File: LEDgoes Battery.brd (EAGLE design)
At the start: 36.8 x 54 mm, 29 parts, among them U1 TPS61032

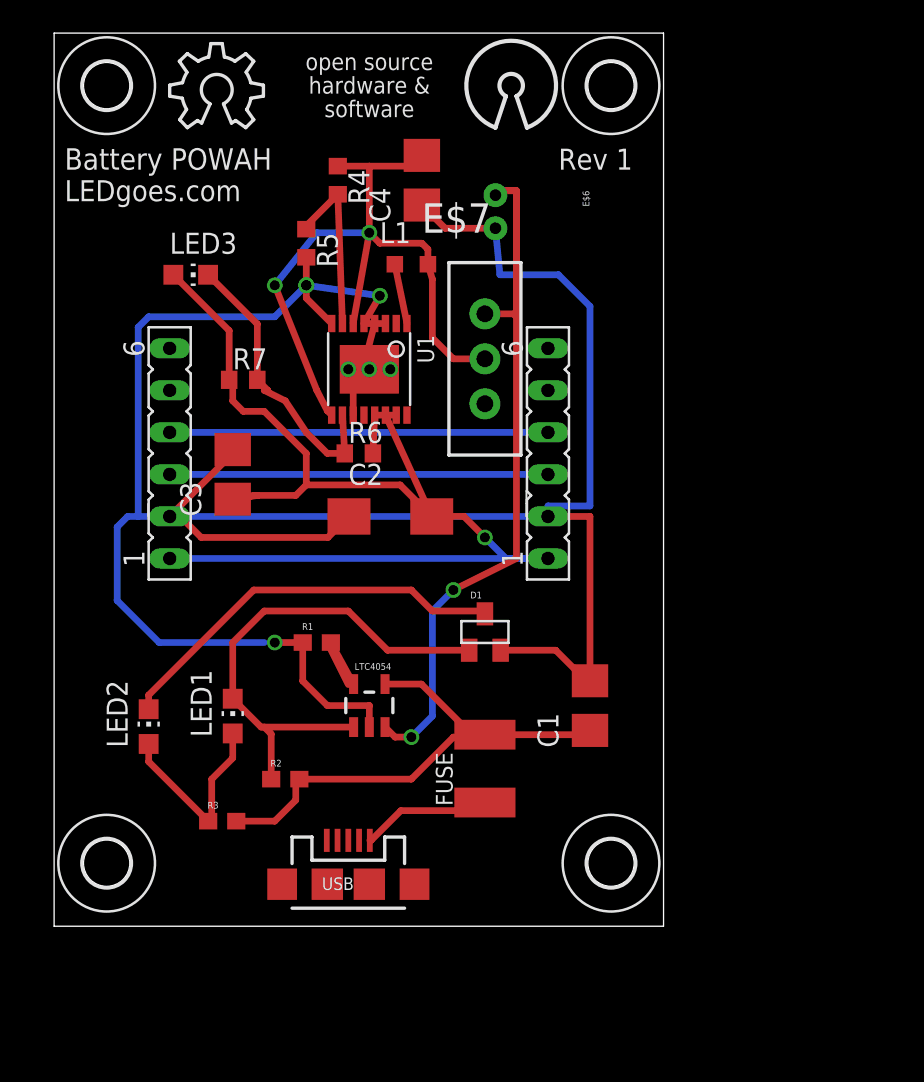
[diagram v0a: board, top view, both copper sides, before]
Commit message: Revision 1 - First Production Revision
Passed design review check 3/2/14
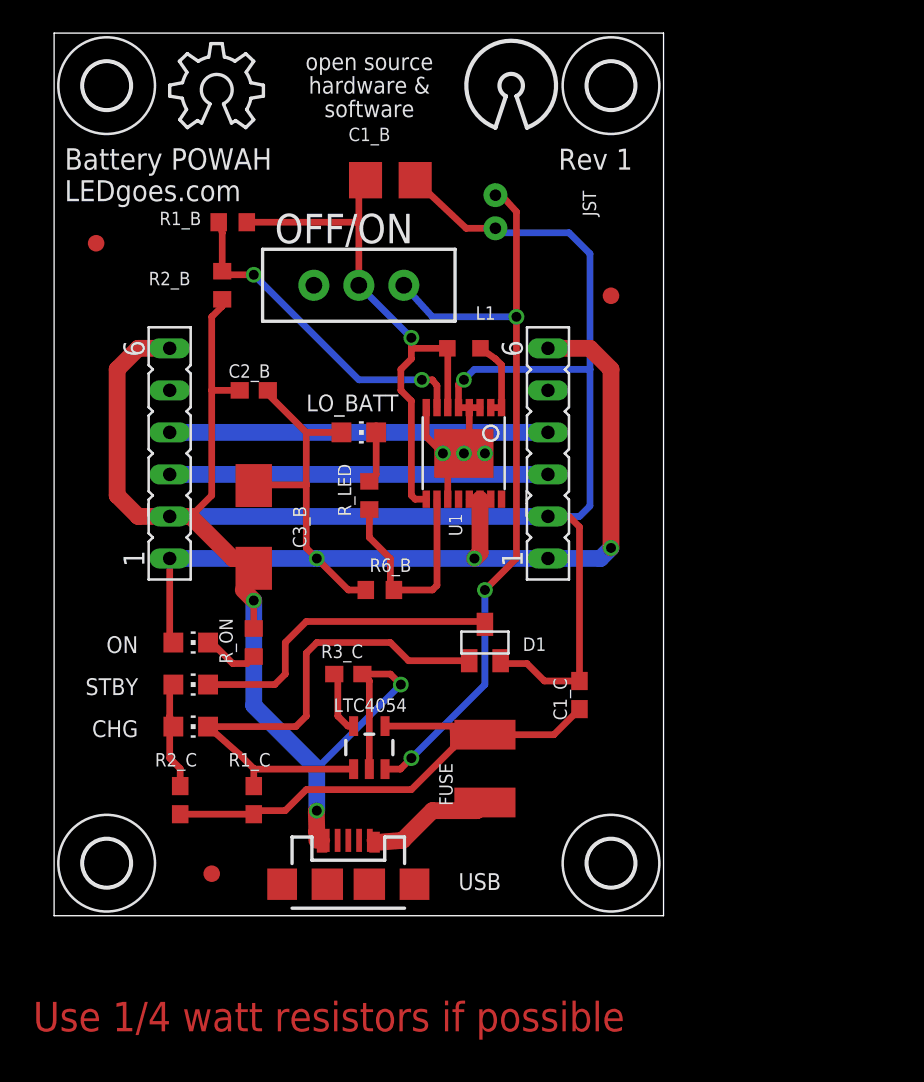
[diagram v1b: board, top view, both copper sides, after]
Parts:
- removed C1: 1uf, rcl:CT3528
- removed C2: 220uF, ref-packages:CT6032
- removed C3: 2.2uf, ref-packages:CT3528
- removed C4: 10uf, ref-packages:CT3528
- removed E$7: (no value), SparkFun-Electromechanical:SWITCH-SPDT_KIT
- removed LED1: Charge, led:CHIP-LED0805
- removed LED2: Standby, led:CHIP-LED0805
- removed LED3: Output, led:CHIP-LED0805
- removed R1: 2k, SparkFun-Resistors:0603
- removed R2: 10k, SparkFun-Resistors:0603
- removed R3: 1k, SparkFun-Resistors:0603
- removed R4, R5, R6, R7: (no value), eagle-ltspice:R0603
- added C1_B: 10uf, ref-packages:CT3528
- added C1_C: 1uf, adafruit:C0603
- added C2_B: 2.2uf, adafruit:C0603
- added C3_B: 220uF, ref-packages:CT6032
- added CHG, LO_BATT, ON, STBY: (no value), led:CHIP-LED0805
- added E$10, E$8, E$9: (no value), adafruit:FIDUCIAL_1MM
- added OFF/ON: (no value), SparkFun-Electromechanical:SWITCH-SPDT_KIT
- added R1_B, R2_B, R6_B, R_LED, R_ON: (no value), eagle-ltspice:R0603
- added R1_C: 10k, SparkFun-Resistors:0603
- added R2_C: 1k, SparkFun-Resistors:0603
- added R3_C: 2k, SparkFun-Resistors:0603
- moved U1 7.65 mm to (25.4, 29.2)
- moved L1 5.99 mm to (25.4, 35.6), turned to 180 degrees
- moved LTC4054 2.54 mm to (19.7, 11.4)
- moved D1 0.63 mm to (26.7, 17.8)
- renumbered E$6 to JST
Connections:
- net S$6 renamed S$20
- removed net S$12: LTC4054.3
- removed net S$13: D1.1, LED1.C, LTC4054.1, R2.1
- removed net S$18: R4.2, R5.1, U1.7
- removed net S$19: C4.-, E$7.2, L1.2, R4.1, U1.6, U1.9
- removed net S$21: L1.1, U1.1
- removed net S$22: C1.-, C2.+, C3.-, C4.+, D1.2, JST.2, LTC4054.2, R1.1, R5.2, U1.11, U1.3, U1.4, U1.5, U1.8, U1.EXP, _.2, __.2
- removed net S$27: C2.-, C3.+, LED3.A, R6.2, R7.1, U1.13, U1.14, U1.15, _.1, __.1
- removed net S$28: LED3.C, R6.1, R7.2, U1.10
- new net /CHRG: CHG.C, D1.1, LTC4054.1, R1_C.1
- new net EN: C1_B.-, L1.2, OFF/ON.2, R1_B.1, U1.6, U1.9
- new net GND: C1_B.+, C1_C.2, C2_B.1, C3_B.+, D1.2, JST.2, LTC4054.2, R2_B.2, R3_C.1, R_ON.2, U1.3, U1.4, U1.5, U1.EXP, USB.VBUS, _.2, _.6, __.2
- new net LBI: R1_B.2, R2_B.1, U1.7
- new net LBO: R6_B.1, R_LED.2, U1.10
- new net S$1: ON.C, R_ON.1
- new net SW: L1.1, U1.1, U1.2
- new net VCC: FUSE.1, USB.GND
- new net VCC_FUSED: C1_C.1, FUSE.2, LTC4054.4, R1_C.2, R2_C.2
- new net VOUT: C2_B.2, C3_B.-, LO_BATT.A, ON.A, R6_B.2, U1.13, U1.14, U1.15, _.1, __.1, __.6
- net S$10: now also LO_BATT.C, R_LED.1; no longer C1.+, FUSE.2, LTC4054.4, R2.2, R3.2
- net S$11: now also R3_C.2; no longer R1.2
- net S$15: now also CHG.A, R2_C.1, STBY.A; no longer LED1.A, LED2.A, R3.1
- net S$16: now also STBY.C; no longer LED2.C
- net S$24: now also LTC4054.3, OFF/ON.1; no longer E$7.1
- net S$8: now also U1.11, U1.8; no longer FUSE.1, USB.GND
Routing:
- net GND: track 0.00 -> 157.3 mm, vias 0 -> 4
- net S$22: track 157.3 -> 0.00 mm, vias 2 -> 0
- net VOUT: track 0.00 -> 72.7 mm, vias 0 -> 3
- net S$27: track 72.7 -> 0.00 mm, vias 1 -> 0
- net S$19: track 43.8 -> 0.00 mm, vias 2 -> 0
- net S$12: track 38.3 -> 0.00 mm, vias 2 -> 0
- net S$24: track 11.0 -> 46.9 mm, vias 0 -> 3
- net EN: track 0.00 -> 34.6 mm, vias 0 -> 1
- net VCC_FUSED: track 0.00 -> 31.9 mm
- net /CHRG: track 0.00 -> 31.4 mm
- net S$13: track 30.8 -> 0.00 mm
- net S$10: track 30.2 -> 3.55 mm
- net LBI: track 0.00 -> 20.2 mm, vias 0 -> 2
- net S$28: track 17.6 -> 0.00 mm
- net LBO: track 0.00 -> 13.4 mm
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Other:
- board size 36.8 x 54 mm -> 36.8 x 53.3 mm
- board text added: "Use 1/4 watt resistors if possible"
